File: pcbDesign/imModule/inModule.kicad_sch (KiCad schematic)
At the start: 6 parts, among them J1 luat-esp32-c3_socket, SW1 SW_DIP_x01, SW2 SW_DIP_x01

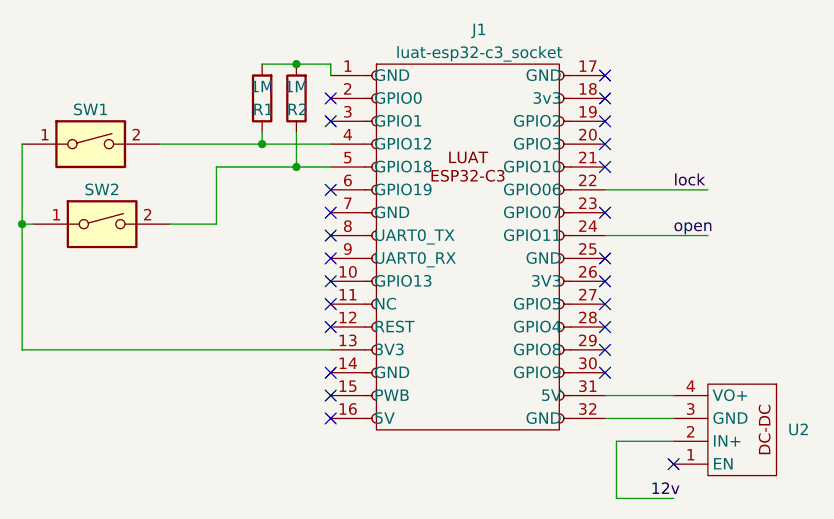
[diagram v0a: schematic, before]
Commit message: update inModule pcb add relay holes
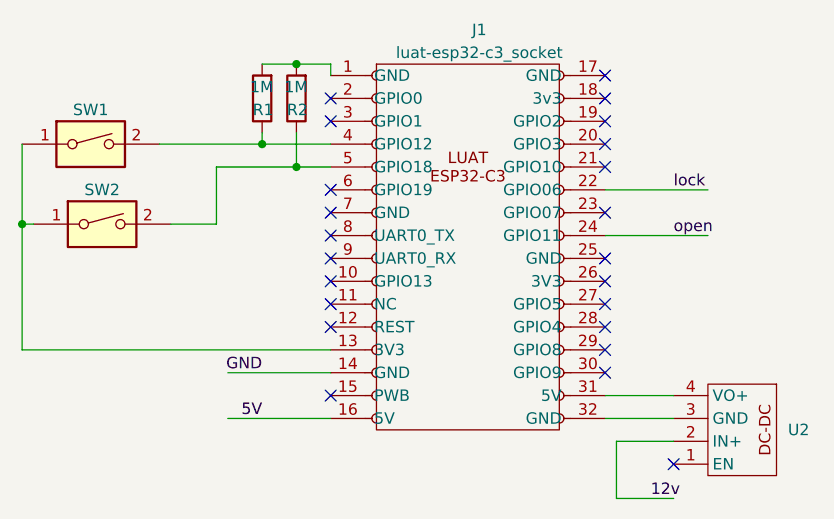
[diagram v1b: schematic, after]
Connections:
- net GND: now reaches J1.14 (GND)
- net 5V: now reaches J1.16 (5V)
- no-connect marks 25 -> 23
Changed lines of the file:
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@@
   (no_connect (at 147.32 109.22))
   (no_connect (at 116.84 93.98))
-  (no_connect (at 116.84 111.76))
   (no_connect (at 116.84 81.28))
   (no_connect (at 116.84 96.52))
@@
   (no_connect (at 147.32 93.98))
   (no_connect (at 116.84 106.68))
-  (no_connect (at 116.84 116.84))
   (no_connect (at 147.32 86.36))
+  (wire (pts (xy 116.84 111.76) (xy 105.41 111.76))
+    (stroke (width 0) (type default))
+  )
   (wire (pts (xy 97.79 86.36) (xy 109.22 86.36))
     (stroke (width 0) (type default))
@@
     (stroke (width 0) (type default))
   )
+  (wire (pts (xy 116.84 116.84) (xy 105.41 116.84))
+    (stroke (width 0) (type default))
+  )
   (wire (pts (xy 113.03 85.09) (xy 113.03 88.9))
     (stroke (width 0) (type default))
@@
   (wire (pts (xy 104.14 95.25) (xy 99.06 95.25))
     (stroke (width 0) (type default))
+  )
+  (label "GND" (at 109.22 111.76 180) (fields_autoplaced)
+    (effects (font (size 1.27 1.27)) (justify right bottom))
+  )
+  (label "5V" (at 109.22 116.84 180) (fields_autoplaced)
+    (effects (font (size 1.27 1.27)) (justify right bottom))
   )
   (label "open" (at 154.94 96.52 0) (fields_autoplaced)
@@
     (pin "2")
     (instances
-      (project "exModule"
+      (project "inModule"
         (path "/0aa07840-b24c-424d-9f30-2f49b25e9449"
           (reference "R1") (unit 1)
@@
     (pin "2")
     (instances
-      (project "exModule"
+      (project "inModule"
         (path "/0aa07840-b24c-424d-9f30-2f49b25e9449"
           (reference "SW2") (unit 1)
@@
     (pin "9")
     (instances
-      (project "exModule"
+      (project "inModule"
         (path "/0aa07840-b24c-424d-9f30-2f49b25e9449"
           (reference "J1") (unit 1)
@@
     (pin "4")
     (instances
-      (project "exModule"
+      (project "inModule"
         (path "/0aa07840-b24c-424d-9f30-2f49b25e9449"
           (reference "U2") (unit 1)
@@
     (pin "2")
     (instances
-      (project "exModule"
+      (project "inModule"
         (path "/0aa07840-b24c-424d-9f30-2f49b25e9449"
           (reference "SW1") (unit 1)
@@
     (pin "2")
     (instances
-      (project "exModule"
+      (project "inModule"
         (path "/0aa07840-b24c-424d-9f30-2f49b25e9449"
           (reference "R2") (unit 1)

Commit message: uodate inModule change gpio define
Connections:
- net open: now also J1.23 (GPIO07); no longer J1.24 (GPIO11)
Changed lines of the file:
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@@
   (no_connect (at 116.84 91.44))
   (no_connect (at 147.32 104.14))
+  (no_connect (at 147.32 96.52))
   (no_connect (at 147.32 88.9))
-  (no_connect (at 147.32 93.98))
   (no_connect (at 116.84 106.68))
   (no_connect (at 147.32 86.36))
@@
     (stroke (width 0) (type default))
   )
-  (wire (pts (xy 147.32 96.52) (xy 158.75 96.52))
+  (wire (pts (xy 82.55 86.36) (xy 82.55 95.25))
     (stroke (width 0) (type default))
   )
-  (wire (pts (xy 82.55 86.36) (xy 82.55 95.25))
+  (wire (pts (xy 147.32 93.98) (xy 158.75 93.98))
     (stroke (width 0) (type default))
   )
@@
     (effects (font (size 1.27 1.27)) (justify right bottom))
   )
+  (label "open" (at 154.94 93.98 0) (fields_autoplaced)
+    (effects (font (size 1.27 1.27)) (justify left bottom))
+  )
   (label "5V" (at 109.22 116.84 180) (fields_autoplaced)
     (effects (font (size 1.27 1.27)) (justify right bottom))
   )
-  (label "open" (at 154.94 96.52 0) (fields_autoplaced)
-    (effects (font (size 1.27 1.27)) (justify left bottom))
-  )
   (label "lock" (at 154.94 91.44 0) (fields_autoplaced)
